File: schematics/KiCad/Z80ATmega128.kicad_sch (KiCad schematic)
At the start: 64 parts, among them J1 AVR-ISP-6, J2 DC 5V, J3 DC 5V, J4 Z80[1..20], J5 Z80[21..40], SW1 Power, U1 74HC125, U10 74HC08, U11 74HC32, U12 74HC32, U13 74LS08, U14 74LS32, U15 74HC74, U2 74HC04, U3 74AC573, U4 74HCT574, U5 AE-CH340E-TYPEC, U6 74HC125, U7 74HC244, U8 74HCT245, U9 AE-CH340E-TYPEC, Y1 16MHz

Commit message: Bug fix of /BUSACK handling during Z80 /RESET is low at power on/manual reset.
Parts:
- renumbered C2 to C1, C11 to C10, C12 to C11, C13 to C12, C14 to C13, C15 to C14, C16 to C15, C17 to C16, C10 to C17, C1 to C2, U9 to U10, U10 to U11, U11 to U12, U12 to U13, U13 to U9
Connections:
- net GND: now also U1.9; no longer U9.12, U9.13
- net /BUSACK: now also U9.11; no longer U1.8
- net /Z80_RESET: now also U9.13
- net at CPU1.23 (~{BUSACK}), R11.2, U2.13: now also U9.12; no longer U1.9
- net /INTRQ renamed /INT4
- net /IORD renamed /INT0
- net /IOWR renamed /INT1
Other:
- moved on the sheet: C1, C10, C11, C12, C13, C14, C15, C16, C17, CPU1, D1, R10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

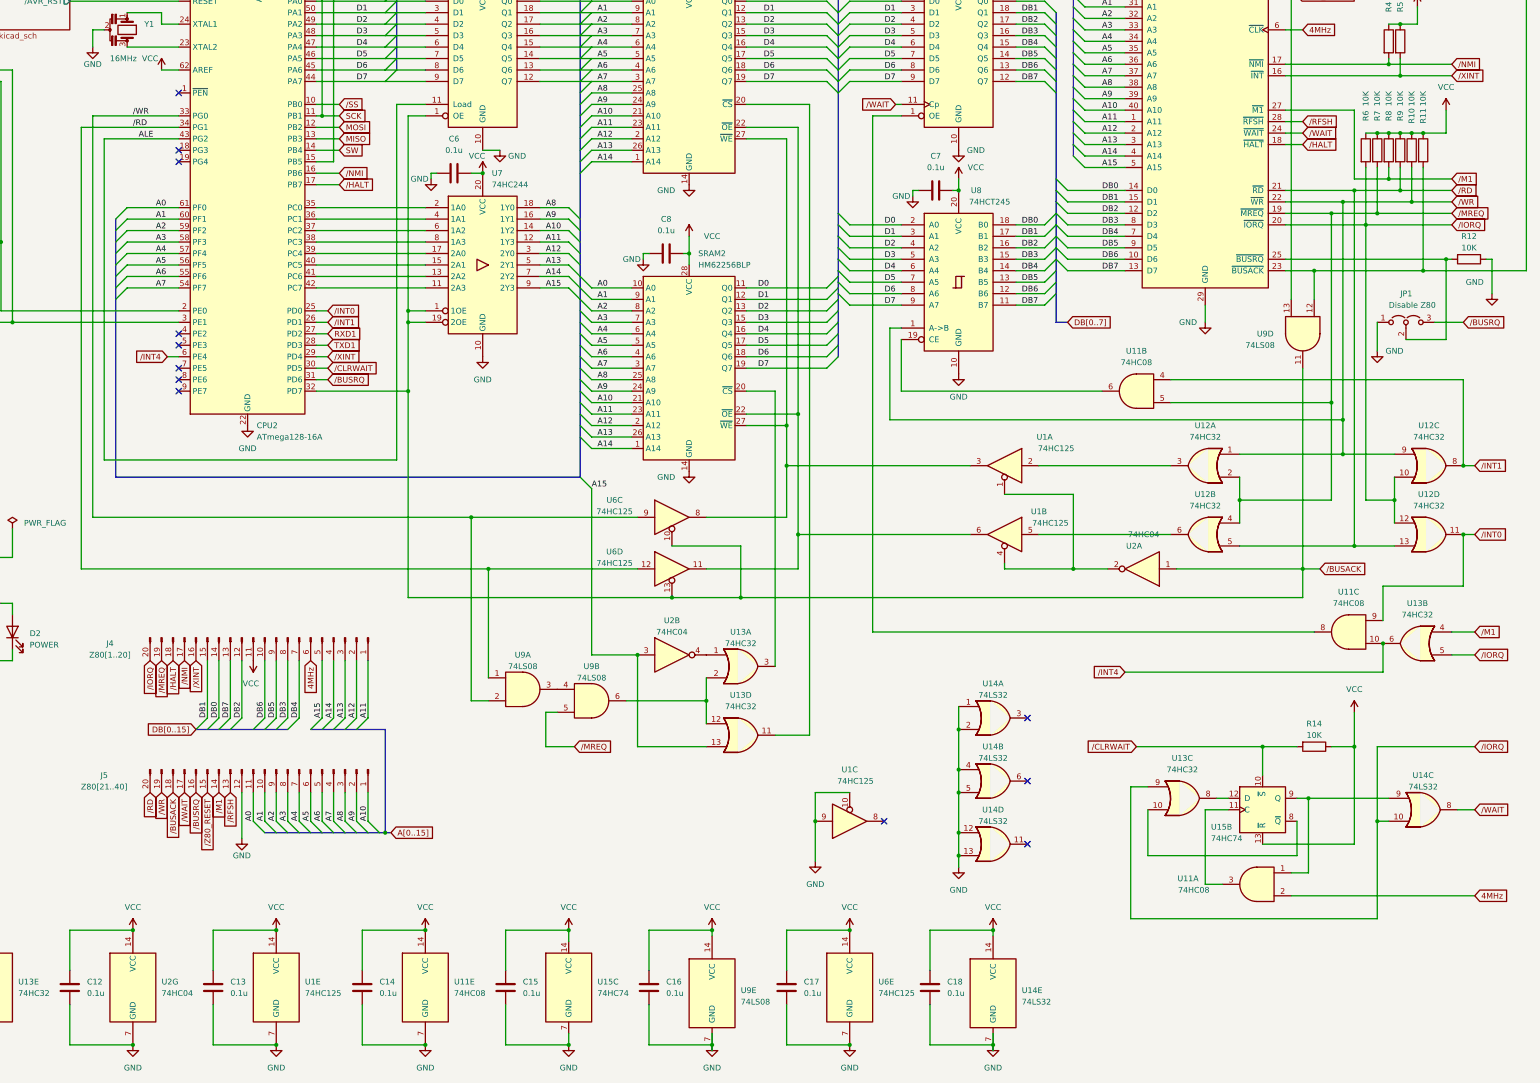
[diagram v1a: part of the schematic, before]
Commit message: Define /WAIT_0 for IOREAD and INT
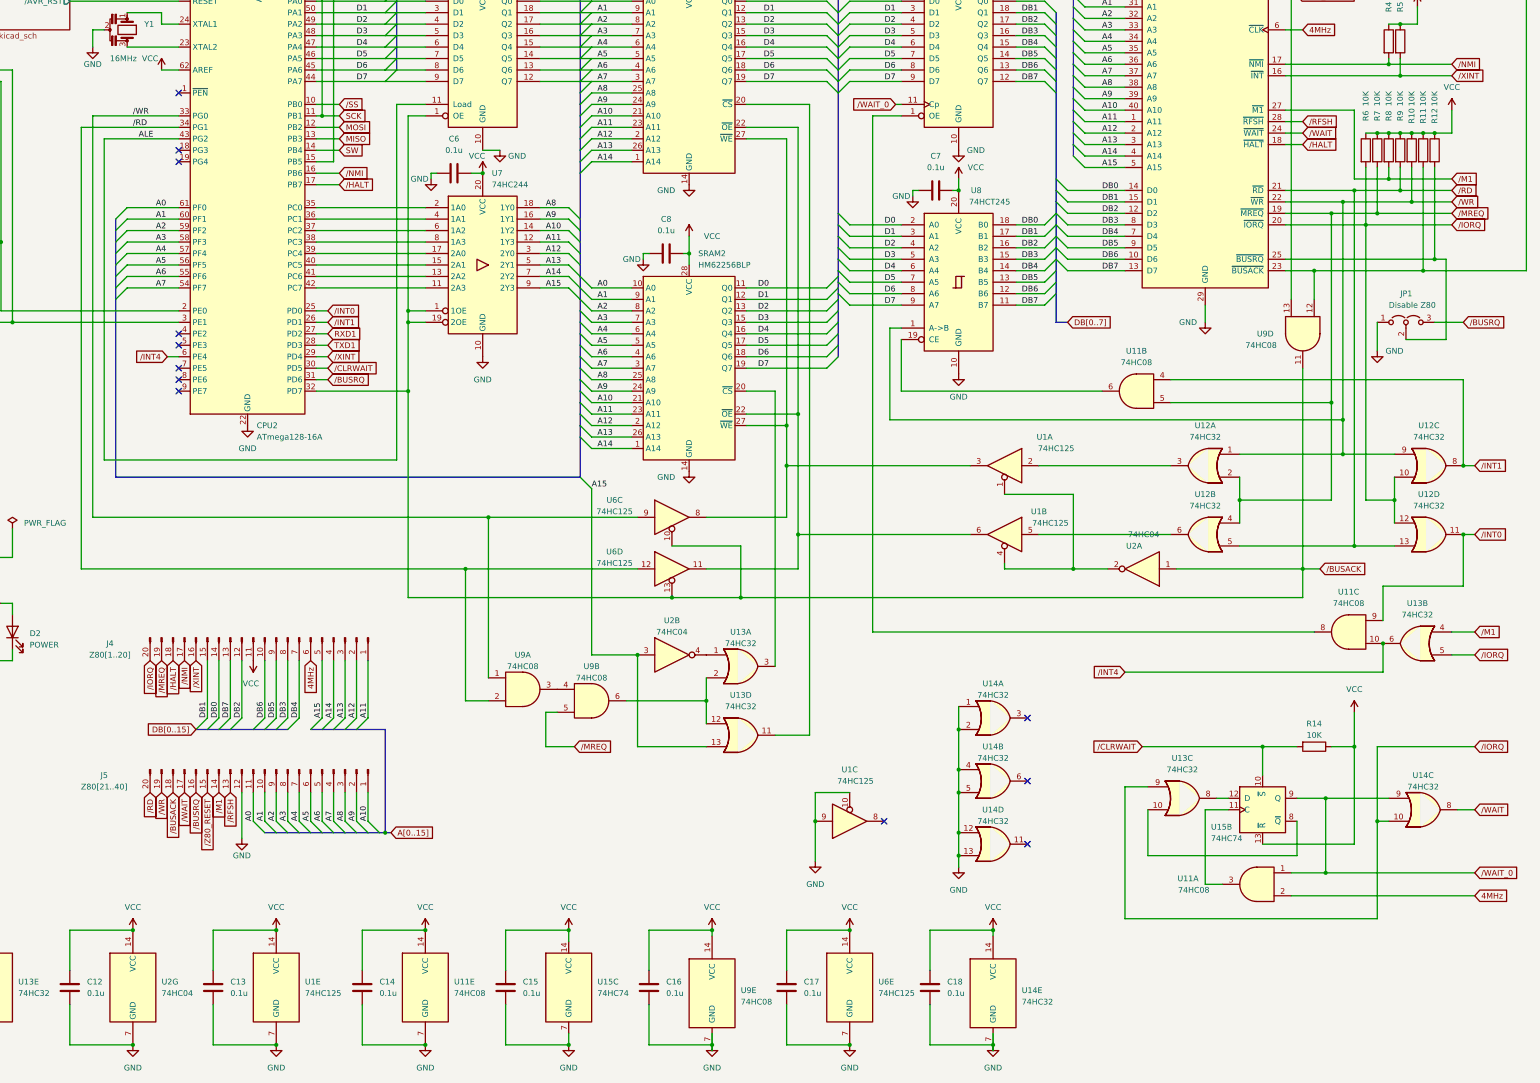
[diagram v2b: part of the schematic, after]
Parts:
- U14: value 74LS32 -> 74HC32; footprint (none) -> Package_DIP:DIP-14_W7.62mm_Socket
- U9: value 74LS08 -> 74HC08
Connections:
- net GND: no longer R12.1
- net VCC: now also R12.1
- net /RD: now also U9.2; no longer U9.1
- net /WAIT: no longer U4.11 (Cp)
- net /WR: now also U9.1; no longer U9.2
- net /WAIT_0: now reaches U11.1, U14.9, U15.9 (Q)
- net /WAIT_0: now also U4.11 (Cp)
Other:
- title: Z80 / ATmega128 Board -> Z80-ATmega128 Board

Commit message: Fixed the comment about the pull up register of ISP RST.
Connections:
- net /M1: now also R10.2; no longer R8.2
- net /WR: now also R8.2; no longer R10.2
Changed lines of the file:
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@@
   (junction (at 303.53 26.67) (diameter 0) (color 0 0 0 0)
   )
+  (junction (at 373.38 90.17) (diameter 0) (color 0 0 0 0)
+  )
   (junction (at 59.69 91.44) (diameter 0) (color 0 0 0 0)
   )
@@
   (junction (at 137.16 71.12) (diameter 0) (color 0 0 0 0)
   )
-  (junction (at 373.38 85.09) (diameter 0) (color 0 0 0 0)
-  )
   (junction (at 120.65 35.56) (diameter 0) (color 0 0 0 0)
   )
@@
   (junction (at 127 251.46) (diameter 0) (color 0 0 0 0)
   )
-  (junction (at 378.46 90.17) (diameter 0) (color 0 0 0 0)
-  )
   (junction (at 191.77 276.86) (diameter 0) (color 0 0 0 0)
   )
@@
   )
   (junction (at 38.1 138.43) (diameter 0) (color 0 0 0 0)
+  )
+  (junction (at 378.46 85.09) (diameter 0) (color 0 0 0 0)
   )
   (junction (at 54.61 179.07) (diameter 0) (color 0 0 0 0)
@@
     (stroke (width 0) (type default))
   )
+  (wire (pts (xy 373.38 82.55) (xy 373.38 90.17))
+    (stroke (width 0) (type default))
+  )
   (wire (pts (xy 54.61 179.07) (xy 58.42 179.07))
     (stroke (width 0) (type default))
@@
     (stroke (width 0) (type default))
   )
-  (wire (pts (xy 365.76 85.09) (xy 373.38 85.09))
-    (stroke (width 0) (type default))
-  )
   (wire (pts (xy 66.04 179.07) (xy 68.58 179.07))
     (stroke (width 0) (type default))
@@
     (stroke (width 0) (type default))
   )
-  (wire (pts (xy 363.22 90.17) (xy 378.46 90.17))
+  (wire (pts (xy 363.22 90.17) (xy 373.38 90.17))
     (stroke (width 0) (type default))
   )
@@
     (stroke (width 0) (type default))
   )
+  (wire (pts (xy 378.46 85.09) (xy 387.35 85.09))
+    (stroke (width 0) (type default))
+  )
   (bus (pts (xy 153.67 45.72) (xy 153.67 48.26))
     (stroke (width 0) (type default))
@@
     (stroke (width 0) (type default))
   )
-  (wire (pts (xy 373.38 85.09) (xy 387.35 85.09))
+  (wire (pts (xy 365.76 85.09) (xy 378.46 85.09))
     (stroke (width 0) (type default))
   )
@@
     (stroke (width 0) (type default))
   )
-  (wire (pts (xy 378.46 90.17) (xy 387.35 90.17))
+  (wire (pts (xy 373.38 90.17) (xy 387.35 90.17))
     (stroke (width 0) (type default))
   )
@@
     (stroke (width 0) (type default))
   )
-  (wire (pts (xy 373.38 85.09) (xy 373.38 82.55))
-    (stroke (width 0) (type default))
-  )
   (wire (pts (xy 231.14 111.76) (xy 248.92 111.76))
     (stroke (width 0) (type default))
@@
     (stroke (width 0) (type default))
   )
-  (wire (pts (xy 378.46 82.55) (xy 378.46 90.17))
+  (wire (pts (xy 378.46 82.55) (xy 378.46 85.09))
     (stroke (width 0) (type default))
   )
@@
     (stroke (width 0) (type default))
   )
-  (text_box "Must be > 470Ω"
+  (text_box "Must be > 4.7KΩ"
     (at 24.13 33.02 0) (size 19.05 3.81)
     (stroke (width 0) (type default))

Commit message: Update schematics to support LED and DIP SW.
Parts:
- removed D1: Z80 active, LED_THT:LED_D3.0mm, symbol Device:LED
- removed R2: 1K, Resistor_THT:R_Axial_DIN0204_L3.6mm_D1.6mm_P7.62mm_Horizontal, symbol Device:R
- removed unit 3 of U1
- removed U10, U5: AE-CH340E-TYPEC, Connector_PinHeader_2.54mm:PinHeader_1x06_P2.54mm_Vertical, symbol 46nori_Library:AE-CH340E-TYPEC
- removed unit 1 of U14
- removed unit 2 of U14
- removed unit 4 of U14
- removed unit 6 of U2
- SW1: footprint (none) -> Button_Switch_THT:SW_CuK_JS202011CQN_DPDT_Straight
- renumbered C18 to C17, C17 to C18, D2 to D1, J4 to J2, J2 to J3, J5 to J4, J3 to J5, R11 to R10, R12 to R11, R14 to R12, R3 to R2, R4 to R3, R5 to R4, R6 to R5, R7 to R6, R8 to R7, R9 to R8, R10 to R9, U12 to U10, U13 to U11, U15 to U12, U14 to U13, U3 to U2, U4 to U3, U2 to U4, U6 to U5, U7 to U6, U8 to U7, U9 to U8, U11 to U9
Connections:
- net /NMI: now also R4.2; no longer R3.2
- net /XINT: now also R3.2; no longer R4.2
- net ExtIO/TXD0: now reaches U5.2
- net /BACK: now reaches CPU1.23 (~{BUSACK}), R10.2, U8.12
- net ExtIO/RXD0: now reaches U5.6
- net ExtIO/DIPSW1: now reaches CPU2.18 (PG3)
- net ExtIO/DIPSW2: now reaches CPU2.19 (PG4)
- net ExtIO/DIPSW3: now reaches CPU2.4 (PE2)
- net ExtIO/DIPSW4: now reaches CPU2.5 (PE3)
- net ExtIO/LED1: now reaches CPU2.7 (PE5)
- net ExtIO/LED2: now reaches CPU2.8 (PE6)
- net ExtIO/LED3: now reaches CPU2.9 (PE7)
- net ExtIO/+5V: now reaches SW1.2 (B)
- no-connect marks 18 -> 3
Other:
- added sheet ExtIO (ExtIO_sch.kicad_sch)
- moved on the sheet: C17, C18, C9, D1, J2, J3, J4, J5, JP2, R13, R3, R4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

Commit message: Pull up ISP CLK by 10K ohm resistor.
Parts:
- added R1: 10K, Resistor_THT:R_Axial_DIN0204_L3.6mm_D1.6mm_P7.62mm_Horizontal, symbol Device:R
- renumbered R9 to R10, R10 to R11, R11 to R12, R12 to R13, R13 to R14, R1 to R2, R2 to R3, R3 to R4, R4 to R5, R5 to R6, R6 to R7, R7 to R8, R8 to R9
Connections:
- net VCC: now also R1.1
- net at J1.3 (SCK), U1.12: now also R1.2
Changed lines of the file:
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@@
   (title_block
     (title "Z80-ATmega128 Board")
-    (date "2023-08-18")
+    (date "2023-08-27")
     (company "By 46nori")
   )
@@
   (junction (at 156.21 114.3) (diameter 0) (color 0 0 0 0)
   )
+  (junction (at 46.99 22.86) (diameter 0) (color 0 0 0 0)
+  )
   (junction (at 251.46 19.05) (diameter 0) (color 0 0 0 0)
   )
@@
   (junction (at 383.54 74.93) (diameter 0) (color 0 0 0 0)
   )
+  (junction (at 25.4 22.86) (diameter 0) (color 0 0 0 0)
+  )
   (junction (at 383.54 48.26) (diameter 0) (color 0 0 0 0)
   )
@@
     (stroke (width 0) (type default))
   )
-  (wire (pts (xy 25.4 24.13) (xy 25.4 30.48))
+  (wire (pts (xy 25.4 19.05) (xy 25.4 22.86))
     (stroke (width 0) (type default))
   )
@@
     (stroke (width 0) (type default))
   )
+  (wire (pts (xy 25.4 22.86) (xy 25.4 30.48))
+    (stroke (width 0) (type default))
+  )
   (wire (pts (xy 27.94 227.33) (xy 27.94 226.06))
     (stroke (width 0) (type default))
@@
     (stroke (width 0) (type default))
   )
+  (wire (pts (xy 25.4 22.86) (xy 30.48 22.86))
+    (stroke (width 0) (type default))
+  )
   (wire (pts (xy 242.57 73.66) (xy 242.57 137.16))
     (stroke (width 0) (type default))
@@
     (stroke (width 0) (type default))
   )
+  (wire (pts (xy 38.1 22.86) (xy 46.99 22.86))
+    (stroke (width 0) (type default))
+  )
   (bus (pts (xy 299.72 63.5) (xy 299.72 66.04))
     (stroke (width 0) (type default))
@@
   (symbol (lib_id "Device:R") (at 375.92 78.74 0) (unit 1)
     (in_bom yes) (on_board yes) (dnp no)
-    (property "Reference" "R8" (at 375.92 71.12 90)
+    (property "Reference" "R9" (at 375.92 71.12 90)
       (effects (font (size 1.27 1.27)))
     )
@@
       (project "Z80ATmega128"
         (path "/8c0ff608-9e5b-458c-8fa7-b9973ff97e88"
-          (reference "R8") (unit 1)
+          (reference "R9") (unit 1)
         )
       )
@@
   (symbol (lib_id "Device:R") (at 383.54 78.74 0) (unit 1)
     (in_bom yes) (on_board yes) (dnp no)
-    (property "Reference" "R11" (at 383.54 71.12 90)
+    (property "Reference" "R12" (at 383.54 71.12 90)
       (effects (font (size 1.27 1.27)))
     )
@@
       (project "Z80ATmega128"
         (path "/8c0ff608-9e5b-458c-8fa7-b9973ff97e88"
-          (reference "R11") (unit 1)
+          (reference "R12") (unit 1)
         )
       )
@@
   (symbol (lib_id "Device:R") (at 87.63 34.29 0) (unit 1)
     (in_bom yes) (on_board yes) (dnp no) (fields_autoplaced)
-    (property "Reference" "R2" (at 90.17 33.0199 0)
+    (property "Reference" "R3" (at 90.17 33.0199 0)
       (effects (font (size 1.27 1.27)) (justify left))
     )
@@
       (project "Z80ATmega128"
         (path "/8c0ff608-9e5b-458c-8fa7-b9973ff97e88"
-          (reference "R2") (unit 1)
+          (reference "R3") (unit 1)
         )
         (path "/8c0ff608-9e5b-458c-8fa7-b9973ff97e88/d23d98f9-7182-4fd3-8808-8c406ff55552"
@@
   (symbol (lib_id "Device:R") (at 383.54 53.34 0) (unit 1)
     (in_bom yes) (on_board yes) (dnp no)
-    (property "Reference" "R4" (at 383.54 44.45 90)
+    (property "Reference" "R5" (at 383.54 44.45 90)
       (effects (font (size 1.27 1.27)))
     )
@@
       (project "Z80ATmega128"
         (path "/8c0ff608-9e5b-458c-8fa7-b9973ff97e88"
-          (reference "R4") (unit 1)
+          (reference "R5") (unit 1)
         )
       )
@@
   (symbol (lib_id "Device:R") (at 373.38 78.74 0) (unit 1)
     (in_bom yes) (on_board yes) (dnp no)
-    (property "Reference" "R7" (at 373.38 71.12 90)
+    (property "Reference" "R8" (at 373.38 71.12 90)
       (effects (font (size 1.27 1.27)))
     )
@@
       (project "Z80ATmega128"
         (path "/8c0ff608-9e5b-458c-8fa7-b9973ff97e88"
-          (reference "R7") (unit 1)
+          (reference "R8") (unit 1)
         )
       )
@@
   (symbol (lib_id "Device:R") (at 370.84 78.74 0) (unit 1)
     (in_bom yes) (on_board yes) (dnp no)
-    (property "Reference" "R6" (at 370.84 71.12 90)
+    (property "Reference" "R7" (at 370.84 71.12 90)
       (effects (font (size 1.27 1.27)))
     )
@@
       (project "Z80ATmega128"
         (path "/8c0ff608-9e5b-458c-8fa7-b9973ff97e88"
-          (reference "R6") (unit 1)
+          (reference "R7") (unit 1)
         )
       )
@@
   (symbol (lib_id "Device:R") (at 356.87 210.82 270) (unit 1)
     (in_bom yes) (on_board yes) (dnp no) (fields_autoplaced)
-    (property "Reference" "R12" (at 356.87 205.74 90)
+    (property "Reference" "R13" (at 356.87 205.74 90)
       (effects (font (size 1.27 1.27)))
     )
@@
       (project "Z80ATmega128"
         (path "/8c0ff608-9e5b-458c-8fa7-b9973ff97e88"
-          (reference "R12") (unit 1)
+          (reference "R13") (unit 1)
         )
         (path "/8c0ff608-9e5b-458c-8fa7-b9973ff97e88/d23d98f9-7182-4fd3-8808-8c406ff55552"
@@
   (symbol (lib_id "Device:R") (at 378.46 78.74 0) (unit 1)
     (in_bom yes) (on_board yes) (dnp no)
-    (property "Reference" "R9" (at 378.46 71.12 90)
+    (property "Reference" "R10" (at 378.46 71.12 90)
       (effects (font (size 1.27 1.27)))
     )
@@
       (project "Z80ATmega128"
         (path "/8c0ff608-9e5b-458c-8fa7-b9973ff97e88"
-          (reference "R9") (unit 1)
+          (reference "R10") (unit 1)
         )
       )
@@
   (symbol (lib_id "Device:R") (at 62.23 214.63 270) (unit 1)
     (in_bom yes) (on_board yes) (dnp no) (fields_autoplaced)
-    (property "Reference" "R13" (at 62.23 208.28 90)
+    (property "Reference" "R14" (at 62.23 208.28 90)
       (effects (font (size 1.27 1.27)))
     )
@@
       (project "Z80ATmega128"
         (path "/8c0ff608-9e5b-458c-8fa7-b9973ff97e88"
-          (reference "R13") (unit 1)
+          (reference "R14") (unit 1)
         )
       )
@@
   (symbol (lib_id "Device:R") (at 381 53.34 0) (unit 1)
     (in_bom yes) (on_board yes) (dnp no)
-    (property "Reference" "R3" (at 381 44.45 90)
+    (property "Reference" "R4" (at 381 44.45 90)
       (effects (font (size 1.27 1.27)))
     )
@@
       (project "Z80ATmega128"
         (path "/8c0ff608-9e5b-458c-8fa7-b9973ff97e88"
-          (reference "R3") (unit 1)
+          (reference "R4") (unit 1)
         )
       )
@@
   (symbol (lib_id "Device:R") (at 381 78.74 0) (unit 1)
     (in_bom yes) (on_board yes) (dnp no)
-    (property "Reference" "R10" (at 381 71.12 90)
+    (property "Reference" "R11" (at 381 71.12 90)
       (effects (font (size 1.27 1.27)))
     )
@@
       (project "Z80ATmega128"
         (path "/8c0ff608-9e5b-458c-8fa7-b9973ff97e88"
-          (reference "R10") (unit 1)
+          (reference "R11") (unit 1)
         )
       )
@@
   (symbol (lib_id "Device:R") (at 34.29 30.48 90) (unit 1)
     (in_bom yes) (on_board yes) (dnp no) (fields_autoplaced)
-    (property "Reference" "R1" (at 34.29 25.4 90)
+    (property "Reference" "R2" (at 34.29 25.4 90)
       (effects (font (size 1.27 1.27)))
     )
@@
       (project "Z80ATmega128"
         (path "/8c0ff608-9e5b-458c-8fa7-b9973ff97e88"
-          (reference "R1") (unit 1)
+          (reference "R2") (unit 1)
         )
         (path "/8c0ff608-9e5b-458c-8fa7-b9973ff97e88/d23d98f9-7182-4fd3-8808-8c406ff55552"
@@
     )
   )
+  (symbol (lib_id "Device:R") (at 34.29 22.86 90) (unit 1)
+    (in_bom yes) (on_board yes) (dnp no) (fields_autoplaced)
+    (property "Reference" "R1" (at 34.29 17.78 90)
+      (effects (font (size 1.27 1.27)))
+    )
+    (property "Value" "10K" (at 34.29 20.32 90)
+      (effects (font (size 1.27 1.27)))
+    )
+    (property "Footprint" "Resistor_THT:R_Axial_DIN0204_L3.6mm_D1.6mm_P7.62mm_Horizontal" (at 34.29 24.638 90)
+      (effects (font (size 1.27 1.27)) hide)
+    )
+    (property "Datasheet" "~" (at 34.29 22.86 0)
+      (effects (font (size 1.27 1.27)) hide)
+    )
+    (pin "1")
+    (pin "2")
+    (instances
+      (project "Z80ATmega128"
+        (path "/8c0ff608-9e5b-458c-8fa7-b9973ff97e88"
+          (reference "R1") (unit 1)
+        )
+        (path "/8c0ff608-9e5b-458c-8fa7-b9973ff97e88/d23d98f9-7182-4fd3-8808-8c406ff55552"
+          (reference "R16") (unit 1)
+        )
+      )
+    )
+  )
   (symbol (lib_id "power:GND") (at 267.97 88.9 0) (unit 1)
     (in_bom yes) (on_board yes) (dnp no)
@@
   (symbol (lib_id "Device:R") (at 368.3 78.74 0) (unit 1)
     (in_bom yes) (on_board yes) (dnp no)
-    (property "Reference" "R5" (at 368.3 71.12 90)
+    (property "Reference" "R6" (at 368.3 71.12 90)
       (effects (font (size 1.27 1.27)))
     )
@@
       (project "Z80ATmega128"
         (path "/8c0ff608-9e5b-458c-8fa7-b9973ff97e88"
-          (reference "R5") (unit 1)
+          (reference "R6") (unit 1)
         )
       )
@@
     )
   )
-  (symbol (lib_id "power:VCC") (at 25.4 24.13 0) (unit 1)
-    (in_bom yes) (on_board yes) (dnp no) (fields_autoplaced)
-    (property "Reference" "#PWR01" (at 25.4 27.94 0)
+  (symbol (lib_id "power:VCC") (at 25.4 19.05 0) (unit 1)
+    (in_bom yes) (on_board yes) (dnp no)
+    (property "Reference" "#PWR01" (at 25.4 22.86 0)
       (effects (font (size 1.27 1.27)) hide)
     )
-    (property "Value" "VCC" (at 25.4 19.05 0)
+    (property "Value" "VCC" (at 25.4 13.97 0)
       (effects (font (size 1.27 1.27)))
     )
-    (property "Footprint" "" (at 25.4 24.13 0)
+    (property "Footprint" "" (at 25.4 19.05 0)
       (effects (font (size 1.27 1.27)) hide)
     )
-    (property "Datasheet" "" (at 25.4 24.13 0)
+    (property "Datasheet" "" (at 25.4 19.05 0)
       (effects (font (size 1.27 1.27)) hide)
     )
